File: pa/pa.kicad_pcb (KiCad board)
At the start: 2 copper layers, 80 x 100 mm, 63 parts, among them J1 Conn_01x02_Pin, J2 Conn_Coaxial, J3 Conn_Coaxial, P1 PMOD-Device-x2-Type-Generic-A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, Q1 Q_NMOS_GSD, Q2 Q_NMOS_GSD, Q3 IRLML6401, Q4 MMBT3904, T1 Transformer_1P_SS, T2 Transformer_1P_SS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

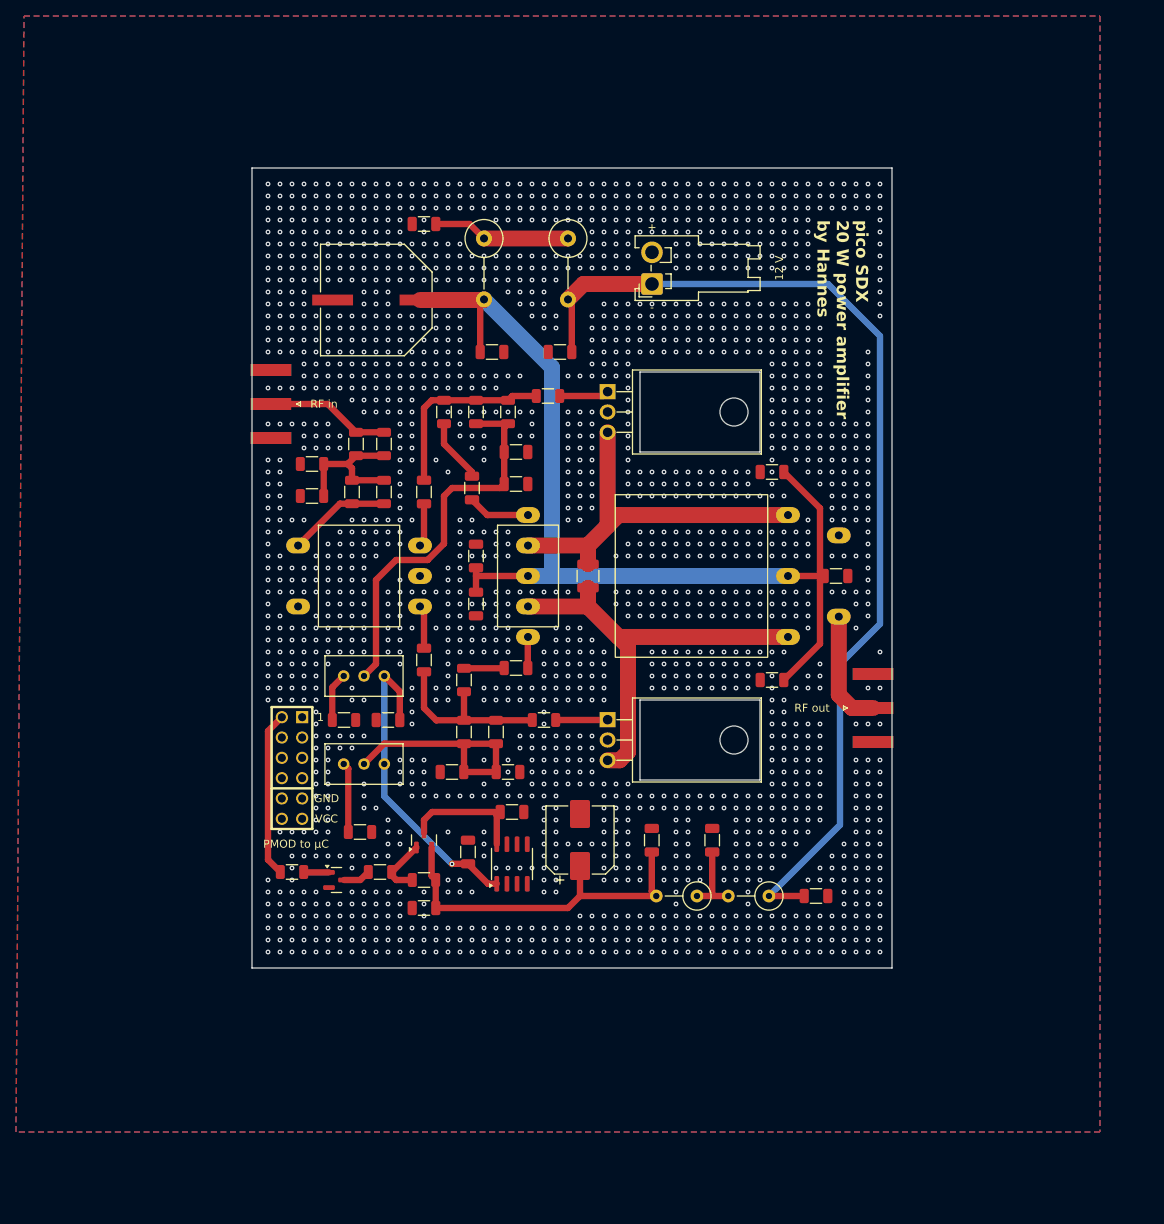
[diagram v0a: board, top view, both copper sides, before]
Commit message: replace 7806 by 1117
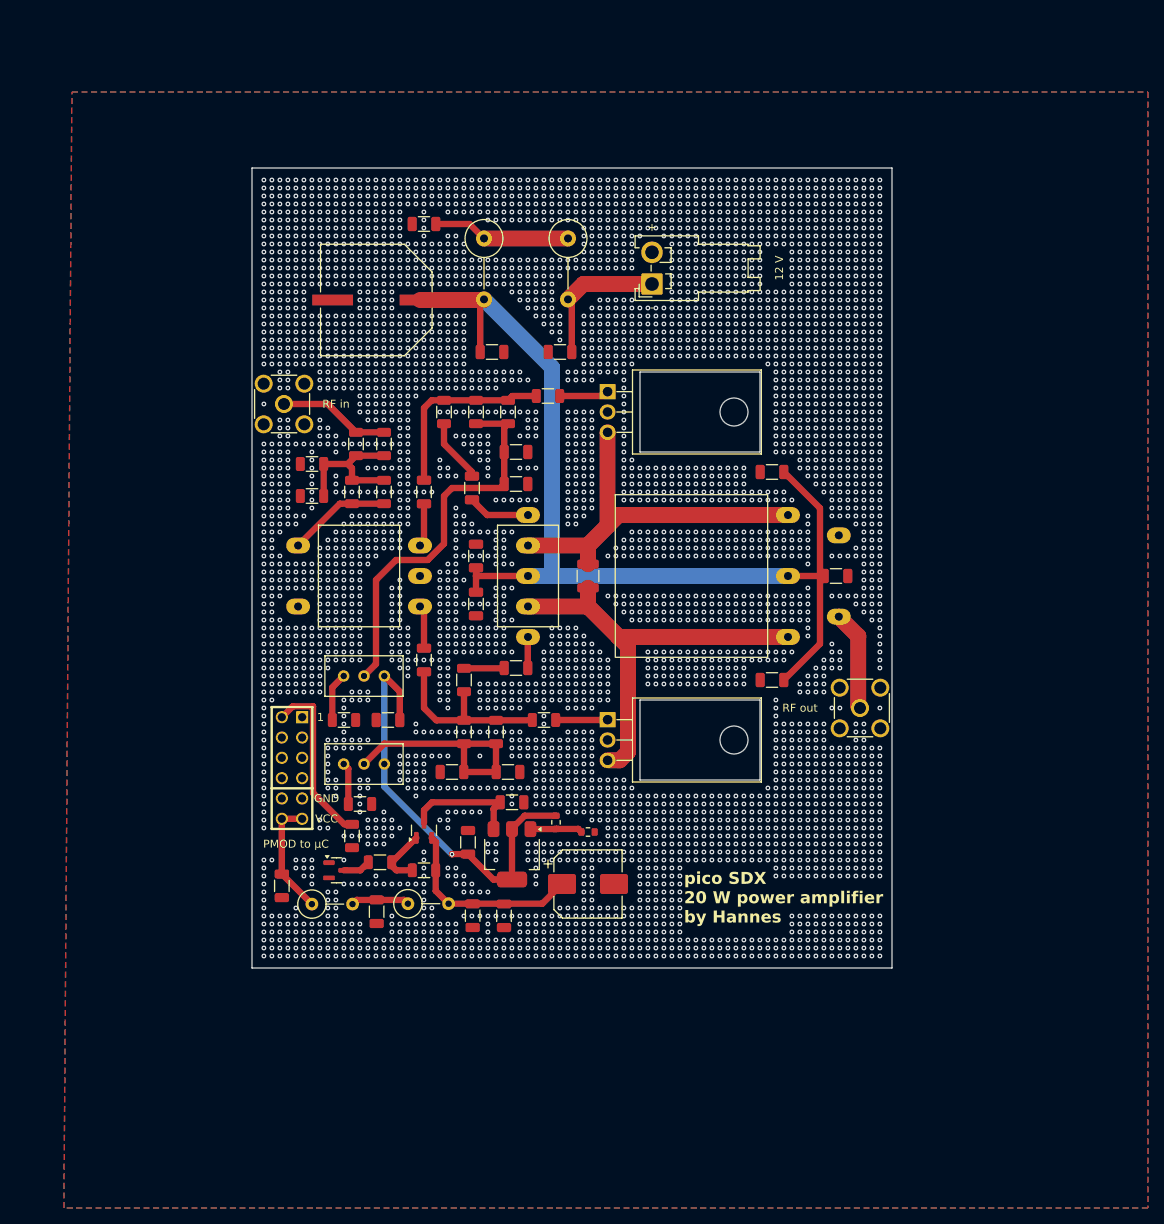
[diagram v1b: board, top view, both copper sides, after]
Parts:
- added R22: R, Resistor_SMD:R_0603_1608Metric, F.Cu at (100.5, 148.3)
- added R23: R, Resistor_SMD:R_0603_1608Metric, F.Cu at (104.5, 149.5)
- J2, J3: footprint Connector_Coaxial:SMA_Amphenol_132289_EdgeMount -> Connector_Coaxial:SMA_Molex_73251-2200_Horizontal
- U1: value L78L06_SO8 -> LT1117-ADJ; footprint Package_SO:SOIC-8_3.9x4.9mm_P1.27mm -> Package_TO_SOT_SMD:SOT-223-3_TabPin2
- moved C26 66.8 mm to (66.2, 156.2), turned to -90 degrees
- moved L4 57.1 mm to (70.0, 158.5), turned to 0 degrees
- moved C23 42.9 mm to (78.1, 159.5), turned to -90 degrees
- moved L3 36.1 mm to (82.0, 158.5), turned to 0 degrees
- moved C22 24.3 mm to (90.1, 160.0), turned to -90 degrees
- moved C24 10.0 mm to (94.0, 160.0), turned to -90 degrees
- moved R20 8.75 mm to (75.0, 150.0), turned to -90 degrees
- moved C25 5.59 mm to (104.5, 156.0), turned to 0 degrees
- moved R18 3.50 mm to (76.0, 146.0)
- moved J2 1.64 mm to (66.5, 96.0), turned to 90 degrees
- moved J3 1.64 mm to (138.5, 134.0), turned to -90 degrees
- moved C20 1.21 mm to (95.0, 145.8)
- moved C21 1.21 mm to (89.5, 150.8)
- moved Q3 1.21 mm to (84.0, 149.3)
- moved Q4 1.21 mm to (73.1, 154.3)
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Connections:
- net +12VA renamed VDDA
- C4 pad 1: +12V -> VDD
- J1 pad 1: +12V -> VDD
- L1 pad 2: +12V -> VDD
- P1 pad 12: unconnected-(P1-P12-Pad12) -> +12V
- P1 pad 6: unconnected-(P1-P6-Pad6) -> +12V
- U1 pad 1: +6V -> Net-(U1-ADJ)
- U1 pad 2: GND -> +6V
- U1 pad 3: GND -> Net-(Q3-D)
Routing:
- net +12V: track 129.4 -> 14.8 mm
- net Net-(Q3-S): track 45.5 -> 24.3 mm
- net VDD: track 0.00 -> 18.1 mm
- net +6V: track 39.9 -> 53.5 mm
- net Net-(U1-ADJ): track 0.00 -> 6.55 mm
- net Net-(R17-Pad3): track 8.74 -> 5.24 mm
- net Net-(Q4-B): track 3.18 -> 0.00 mm
- net Net-(J3-In): track 14.7 -> 12.5 mm
- net Net-(C23-Pad1): track 9.43 -> 7.33 mm
- net Net-(J2-In): track 15.6 -> 14.0 mm
- net TX~{RX}: track 20.7 -> 21.8 mm
- net Net-(Q3-D): track 15.7 -> 15.2 mm
- net GND: vias 1856 -> 4337

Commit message: drc clean
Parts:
- removed Q4: MMBT3904, Package_TO_SOT_SMD:SOT-23
- removed R20: 1.8 kR, Resistor_SMD:R_1206_3216Metric
- moved J2 1.00 mm to (67.5, 96.0)
- moved J3 0.96 mm to (137.5, 134.0)
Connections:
- R21 pad 2: Net-(Q4-C) -> TX~{RX}
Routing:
- net GND: track 0.00 -> 12.0 mm, vias 4337 -> 4341
- net TX~{RX}: track 21.8 -> 26.8 mm
- net Net-(Q4-C): track 3.45 -> 0.00 mm
- net Net-(J2-In): track 14.0 -> 13.0 mm
